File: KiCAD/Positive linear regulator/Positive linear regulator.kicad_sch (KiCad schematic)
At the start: 1 part, among them U1 LM4562

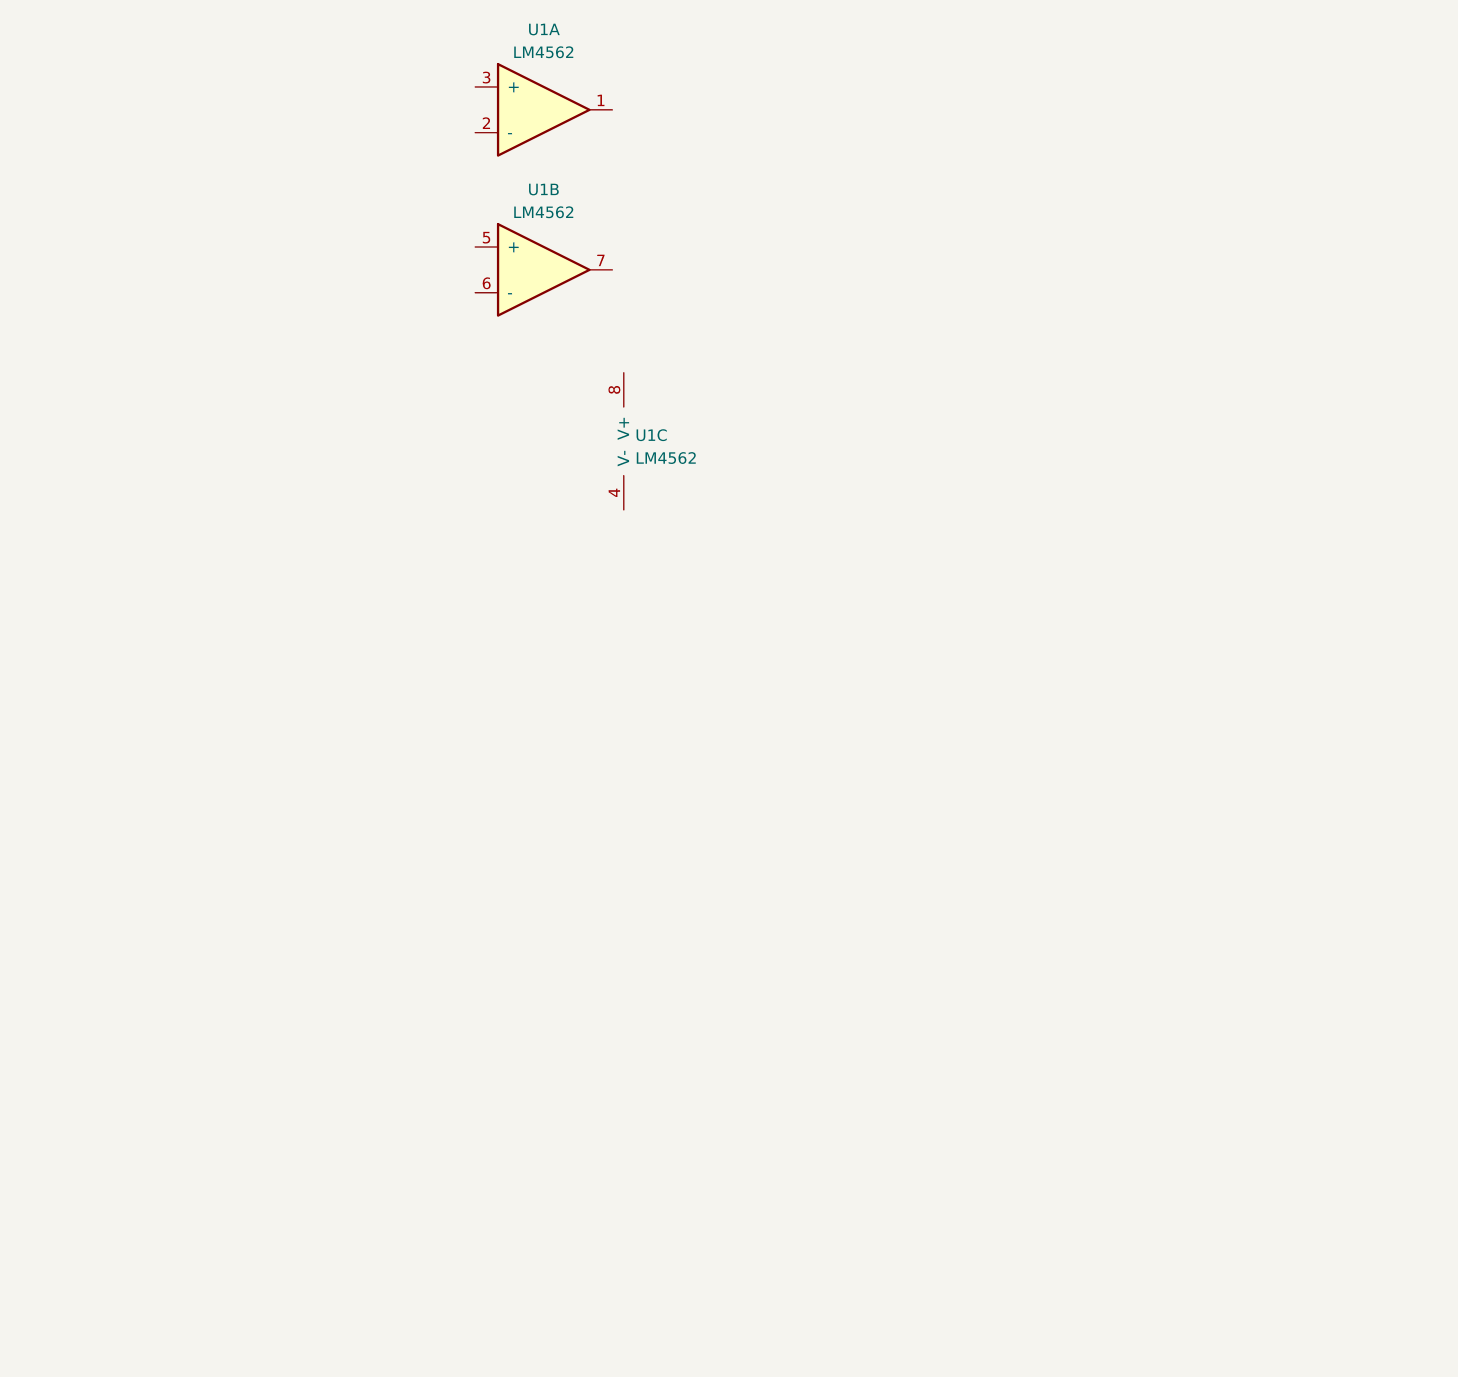
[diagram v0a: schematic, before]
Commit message: Added two components to our KiCAD lib
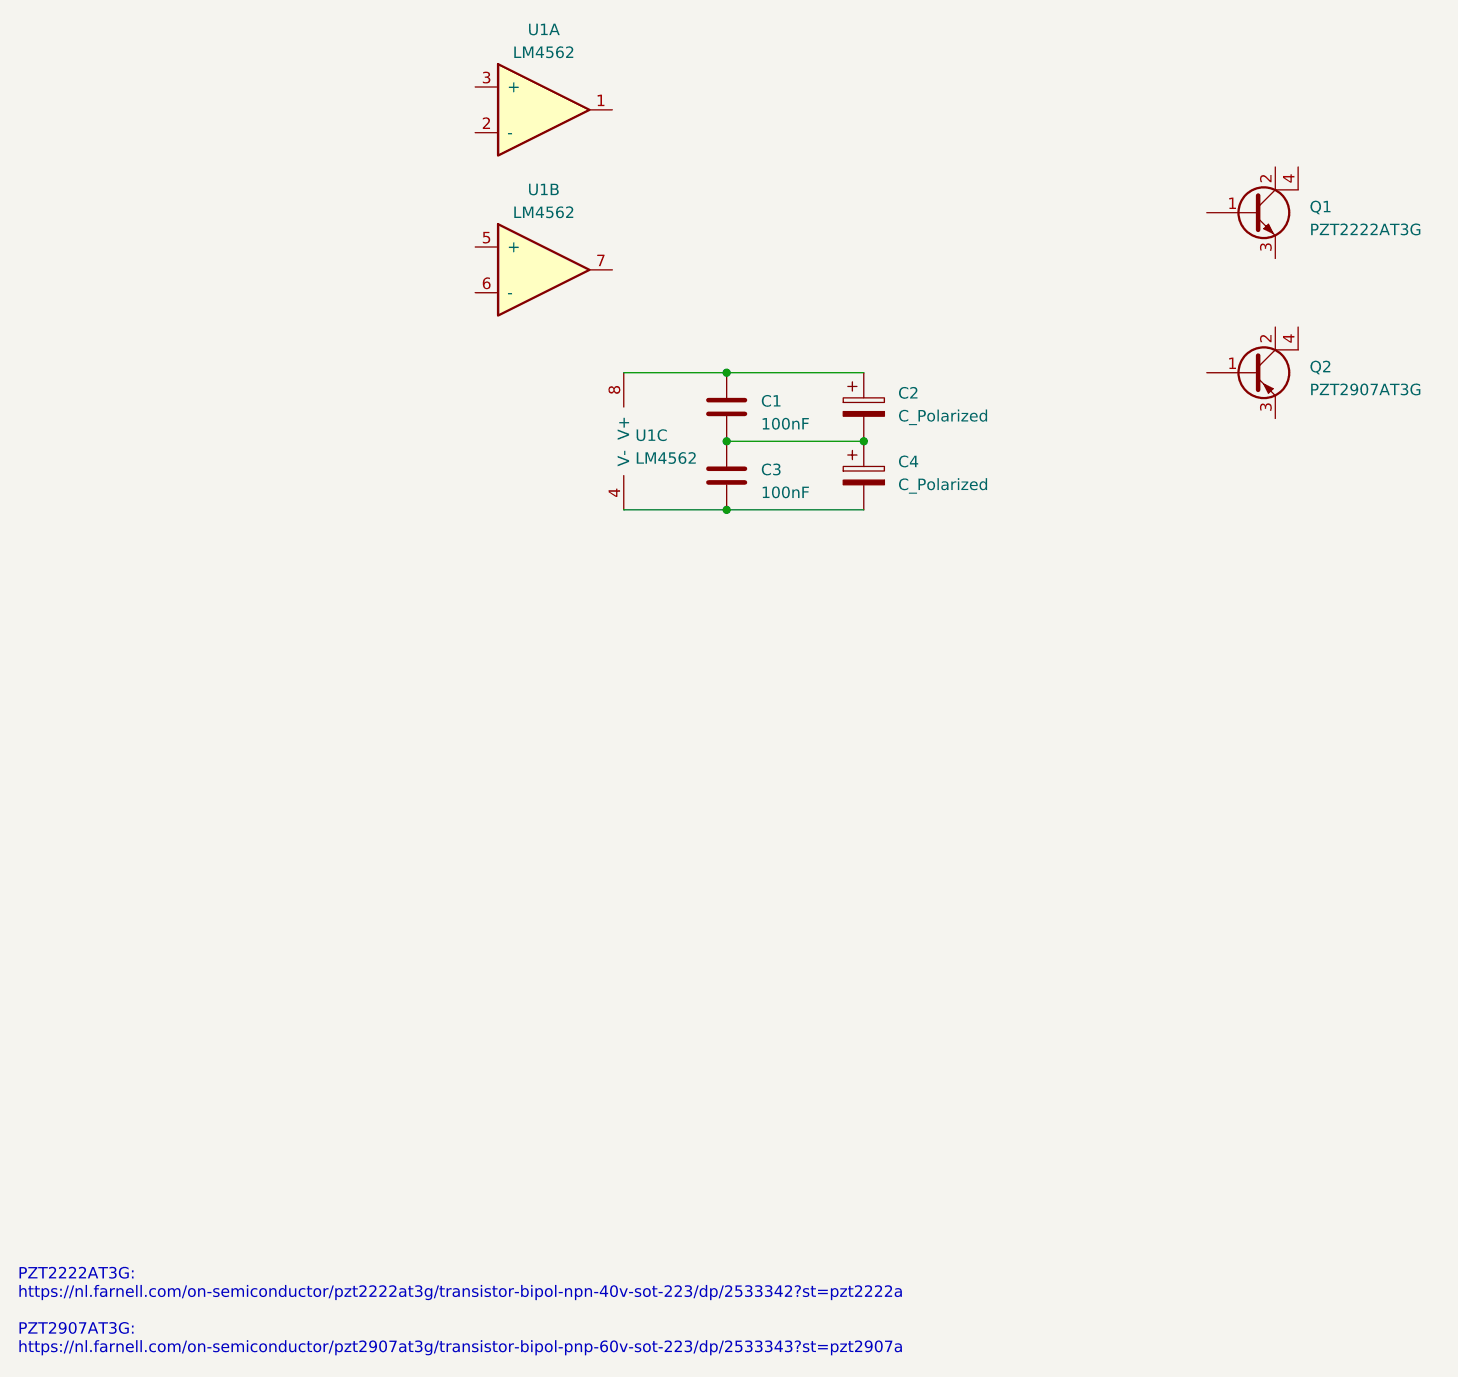
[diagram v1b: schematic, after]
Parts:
- added C1, C3: 100nF, symbol Device:C
- added C2, C4: C_Polarized, symbol Device:C_Polarized
- added Q1: PZT2222AT3G, Package_TO_SOT_SMD:SOT-223, symbol Audio_DSP:PZT2222AT3G
- added Q2: PZT2907AT3G, Package_TO_SOT_SMD:SOT-223, symbol Audio_DSP:PZT2907AT3G
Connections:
- net at U1.4 (V-): now also C3.2, C4.2
- net at U1.8 (V+): now also C1.1, C2.1
- new net: C1.2, C2.2, C3.1, C4.1
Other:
- note added: "PZT2222AT3G: https://nl.farnell.com/on-semiconductor/pzt2222at3g/transistor-bipol-npn-40v-sot-223/dp/2533342?st=pzt2222a PZT2907AT3G: https://nl.farnell.com/on-semiconductor/pzt2907at3g/transistor-bipol-pnp-60v-sot-223/dp/2533343?st=pzt2907a"
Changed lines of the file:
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@@
 (kicad_sch (version 20230121) (generator eeschema)
   (paper "A4")
+  (junction (at 123.19 87.63) (diameter 0) (color 0 0 0 0)
+  )
+  (junction (at 107.95 95.25) (diameter 0) (color 0 0 0 0)
+  )
+  (junction (at 107.95 80.01) (diameter 0) (color 0 0 0 0)
+  )
+  (junction (at 107.95 87.63) (diameter 0) (color 0 0 0 0)
+  )
+  (wire (pts (xy 96.52 95.25) (xy 107.95 95.25))
+    (stroke (width 0) (type default))
+  )
+  (wire (pts (xy 107.95 87.63) (xy 123.19 87.63))
+    (stroke (width 0) (type default))
+  )
+  (wire (pts (xy 96.52 80.01) (xy 107.95 80.01))
+    (stroke (width 0) (type default))
+  )
+  (wire (pts (xy 107.95 95.25) (xy 123.19 95.25))
+    (stroke (width 0) (type default))
+  )
+  (wire (pts (xy 107.95 80.01) (xy 123.19 80.01))
+    (stroke (width 0) (type default))
+  )
+  (text "PZT2222AT3G:\nhttps://nl.farnell.com/on-semiconductor/pzt2222at3g/transistor-bipol-npn-40v-sot-223/dp/2533342?st=pzt2222a\n \nPZT2907AT3G:\nhttps://nl.farnell.com/on-semiconductor/pzt2907at3g/transistor-bipol-pnp-60v-sot-223/dp/2533343?st=pzt2907a"
+    (at 29.21 189.23 0)
+    (effects (font (size 1.27 1.27)) (justify left bottom))
+  )
   (symbol (lib_id "Audio_DSP:LM4562") (at 86.36 50.8 0) (unit 1)
     (in_bom yes) (on_board yes) (dnp no) (fields_autoplaced)
@@
     )
   )
+  (symbol (lib_id "Device:C") (at 107.95 91.44 0) (unit 1)
+    (in_bom yes) (on_board yes) (dnp no) (fields_autoplaced)
+    (property "Reference" "C3" (at 111.76 90.805 0)
+      (effects (font (size 1.27 1.27)) (justify left))
+    )
+    (property "Value" "100nF" (at 111.76 93.345 0)
+      (effects (font (size 1.27 1.27)) (justify left))
+    )
+    (property "Footprint" "" (at 108.9152 95.25 0)
+      (effects (font (size 1.27 1.27)) hide)
+    )
+    (property "Datasheet" "~" (at 107.95 91.44 0)
+      (effects (font (size 1.27 1.27)) hide)
+    )
+    (pin "1")
+    (pin "2")
+    (instances
+      (project "Positive linear regulator"
+        (path "/19504711-657f-4df2-b2e9-322b7e64e4f7"
+          (reference "C3") (unit 1)
+        )
+      )
+    )
+  )
+  (symbol (lib_id "Device:C") (at 107.95 83.82 0) (unit 1)
+    (in_bom yes) (on_board yes) (dnp no) (fields_autoplaced)
+    (property "Reference" "C1" (at 111.76 83.185 0)
+      (effects (font (size 1.27 1.27)) (justify left))
+    )
+    (property "Value" "100nF" (at 111.76 85.725 0)
+      (effects (font (size 1.27 1.27)) (justify left))
+    )
+    (property "Footprint" "" (at 108.9152 87.63 0)
+      (effects (font (size 1.27 1.27)) hide)
+    )
+    (property "Datasheet" "~" (at 107.95 83.82 0)
+      (effects (font (size 1.27 1.27)) hide)
+    )
+    (pin "1")
+    (pin "2")
+    (instances
+      (project "Positive linear regulator"
+        (path "/19504711-657f-4df2-b2e9-322b7e64e4f7"
+          (reference "C1") (unit 1)
+        )
+      )
+    )
+  )
+  (symbol (lib_id "Audio_DSP:PZT2222AT3G") (at 167.64 62.23 0) (unit 1)
+    (in_bom yes) (on_board yes) (dnp no) (fields_autoplaced)
+    (property "Reference" "Q1" (at 172.72 61.595 0)
+      (effects (font (size 1.27 1.27)) (justify left))
+    )
+    (property "Value" "PZT2222AT3G" (at 172.72 64.135 0)
+      (effects (font (size 1.27 1.27)) (justify left))
+    )
+    (property "Footprint" "Package_TO_SOT_SMD:SOT-223" (at 167.64 76.2 0)
+      (effects (font (size 1.27 1.27)) hide)
+    )
+    (property "Datasheet" "https://nl.farnell.com/on-semiconductor/pzt2222at3g/transistor-bipol-npn-40v-sot-223/dp/2533342?st=pzt2222a" (at 167.64 78.74 0)
+      (effects (font (size 1.27 1.27)) hide)
+    )
+    (pin "1")
+    (pin "2")
+    (pin "3")
+    (pin "4")
+    (instances
+      (project "Positive linear regulator"
+        (path "/19504711-657f-4df2-b2e9-322b7e64e4f7"
+          (reference "Q1") (unit 1)
+        )
+      )
+    )
+  )
   (symbol (lib_id "Audio_DSP:LM4562") (at 96.52 87.63 0) (unit 3)
     (in_bom yes) (on_board yes) (dnp no) (fields_autoplaced)
@@
     )
   )
+  (symbol (lib_id "Device:C_Polarized") (at 123.19 91.44 0) (unit 1)
+    (in_bom yes) (on_board yes) (dnp no) (fields_autoplaced)
+    (property "Reference" "C4" (at 127 89.916 0)
+      (effects (font (size 1.27 1.27)) (justify left))
+    )
+    (property "Value" "C_Polarized" (at 127 92.456 0)
+      (effects (font (size 1.27 1.27)) (justify left))
+    )
+    (property "Footprint" "" (at 124.1552 95.25 0)
+      (effects (font (size 1.27 1.27)) hide)
+    )
+    (property "Datasheet" "~" (at 123.19 91.44 0)
+      (effects (font (size 1.27 1.27)) hide)
+    )
+    (pin "1")
+    (pin "2")
+    (instances
+      (project "Positive linear regulator"
+        (path "/19504711-657f-4df2-b2e9-322b7e64e4f7"
+          (reference "C4") (unit 1)
+        )
+      )
+    )
+  )
+  (symbol (lib_id "Audio_DSP:PZT2907AT3G") (at 167.64 80.01 0) (unit 1)
+    (in_bom yes) (on_board yes) (dnp no) (fields_autoplaced)
+    (property "Reference" "Q2" (at 172.72 79.375 0)
+      (effects (font (size 1.27 1.27)) (justify left))
+    )
+    (property "Value" "PZT2907AT3G" (at 172.72 81.915 0)
+      (effects (font (size 1.27 1.27)) (justify left))
+    )
+    (property "Footprint" "Package_TO_SOT_SMD:SOT-223" (at 167.64 93.98 0)
+      (effects (font (size 1.27 1.27)) hide)
+    )
+    (property "Datasheet" "https://nl.farnell.com/on-semiconductor/pzt2907at3g/transistor-bipol-pnp-60v-sot-223/dp/2533343?st=pzt2907a" (at 167.64 96.52 0)
+      (effects (font (size 1.27 1.27)) hide)
+    )
+    (pin "1")
+    (pin "2")
+    (pin "3")
+    (pin "4")
+    (instances
+      (project "Positive linear regulator"
+        (path "/19504711-657f-4df2-b2e9-322b7e64e4f7"
+          (reference "Q2") (unit 1)
+        )
+      )
+    )
+  )
   (symbol (lib_id "Audio_DSP:LM4562") (at 86.36 68.58 0) (unit 2)
     (in_bom yes) (on_board yes) (dnp no) (fields_autoplaced)
@@
         )
       )
+    )
+  )
+  (symbol (lib_id "Device:C_Polarized") (at 123.19 83.82 0) (unit 1)
+    (in_bom yes) (on_board yes) (dnp no) (fields_autoplaced)
+    (property "Reference" "C2" (at 127 82.296 0)
+      (effects (font (size 1.27 1.27)) (justify left))
+    )
+    (property "Value" "C_Polarized" (at 127 84.836 0)
+      (effects (font (size 1.27 1.27)) (justify left))
+    )
+    (property "Footprint" "" (at 124.1552 87.63 0)
+      (effects (font (size 1.27 1.27)) hide)
+    )
+    (property "Datasheet" "~" (at 123.19 83.82 0)
+      (effects (font (size 1.27 1.27)) hide)
+    )
+    (pin "1")
+    (pin "2")
+    (instances
+      (project "Positive linear regulator"
+        (path "/19504711-657f-4df2-b2e9-322b7e64e4f7"
+          (reference "C2") (unit 1)
+        )
+      )

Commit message: Updated file structure
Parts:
- removed C2, C4: C_Polarized, symbol Device:C_Polarized
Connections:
- net GND: now reaches C1.2, C3.1
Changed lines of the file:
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@@
 (kicad_sch (version 20230121) (generator eeschema)
   (paper "A4")
-  (junction (at 123.19 87.63) (diameter 0) (color 0 0 0 0)
-  )
-  (junction (at 107.95 95.25) (diameter 0) (color 0 0 0 0)
-  )
-  (junction (at 107.95 80.01) (diameter 0) (color 0 0 0 0)
-  )
   (junction (at 107.95 87.63) (diameter 0) (color 0 0 0 0)
   )
@@
     (stroke (width 0) (type default))
   )
-  (wire (pts (xy 107.95 87.63) (xy 123.19 87.63))
-    (stroke (width 0) (type default))
-  )
   (wire (pts (xy 96.52 80.01) (xy 107.95 80.01))
-    (stroke (width 0) (type default))
-  )
-  (wire (pts (xy 107.95 95.25) (xy 123.19 95.25))
-    (stroke (width 0) (type default))
-  )
-  (wire (pts (xy 107.95 80.01) (xy 123.19 80.01))
     (stroke (width 0) (type default))
   )
@@
     )
   )
-  (symbol (lib_id "Device:C_Polarized") (at 123.19 91.44 0) (unit 1)
-    (in_bom yes) (on_board yes) (dnp no) (fields_autoplaced)
-    (property "Reference" "C4" (at 127 89.916 0)
-      (effects (font (size 1.27 1.27)) (justify left))
-    )
-    (property "Value" "C_Polarized" (at 127 92.456 0)
-      (effects (font (size 1.27 1.27)) (justify left))
-    )
-    (property "Footprint" "" (at 124.1552 95.25 0)
-      (effects (font (size 1.27 1.27)) hide)
-    )
-    (property "Datasheet" "~" (at 123.19 91.44 0)
-      (effects (font (size 1.27 1.27)) hide)
-    )
-    (pin "1")
-    (pin "2")
-    (instances
-      (project "Positive linear regulator"
-        (path "/19504711-657f-4df2-b2e9-322b7e64e4f7"
-          (reference "C4") (unit 1)
+  (symbol (lib_id "power:GND") (at 107.95 87.63 90) (unit 1)
+    (in_bom yes) (on_board yes) (dnp no) (fields_autoplaced)
+    (property "Reference" "#PWR01" (at 114.3 87.63 0)
+      (effects (font (size 1.27 1.27)) hide)
+    )
+    (property "Value" "GND" (at 111.76 88.265 90)
+      (effects (font (size 1.27 1.27)) (justify right))
+    )
+    (property "Footprint" "" (at 107.95 87.63 0)
+      (effects (font (size 1.27 1.27)) hide)
+    )
+    (property "Datasheet" "" (at 107.95 87.63 0)
+      (effects (font (size 1.27 1.27)) hide)
+    )
+    (pin "1")
+    (instances
+      (project "Positive linear regulator"
+        (path "/19504711-657f-4df2-b2e9-322b7e64e4f7"
+          (reference "#PWR01") (unit 1)
         )
       )
@@
         )
       )
-    )
-  )
-  (symbol (lib_id "Device:C_Polarized") (at 123.19 83.82 0) (unit 1)
-    (in_bom yes) (on_board yes) (dnp no) (fields_autoplaced)
-    (property "Reference" "C2" (at 127 82.296 0)
-      (effects (font (size 1.27 1.27)) (justify left))
-    )
-    (property "Value" "C_Polarized" (at 127 84.836 0)
-      (effects (font (size 1.27 1.27)) (justify left))
-    )
-    (property "Footprint" "" (at 124.1552 87.63 0)
-      (effects (font (size 1.27 1.27)) hide)
-    )
-    (property "Datasheet" "~" (at 123.19 83.82 0)
-      (effects (font (size 1.27 1.27)) hide)
-    )
-    (pin "1")
-    (pin "2")
-    (instances
-      (project "Positive linear regulator"
-        (path "/19504711-657f-4df2-b2e9-322b7e64e4f7"
-          (reference "C2") (unit 1)
-        )
-      )
